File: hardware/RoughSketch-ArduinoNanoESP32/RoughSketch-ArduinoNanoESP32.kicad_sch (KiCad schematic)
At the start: 28 parts, among them J1 Front Panel, K1 Compressor Relay, K2 Auger Relay, M1 Compressor, M2 Auger Motor, M3 Pump, M4 Fan, Q1 Pump Mosfet, Q2 UV LED Mosfet, Q3 Fan Mosfet, Q4 Bin LED Mosfet, Q5 IR LED Mosfet, SW3 Bin Switch, SW4 Float High, SW5 Float Low

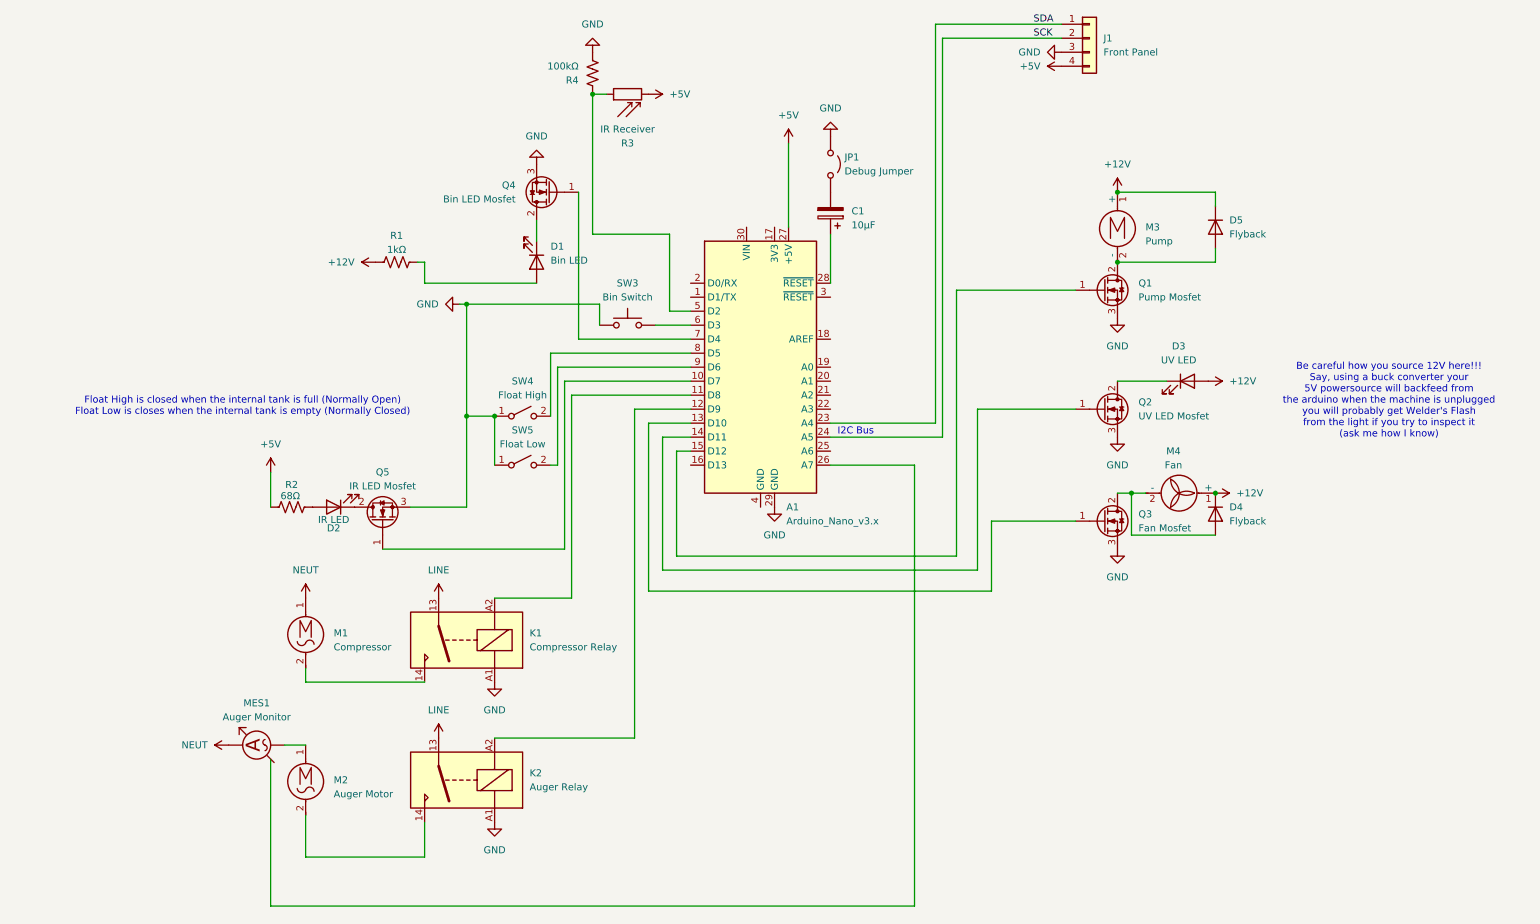
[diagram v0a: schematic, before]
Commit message: Migration from Atmel to ESP32
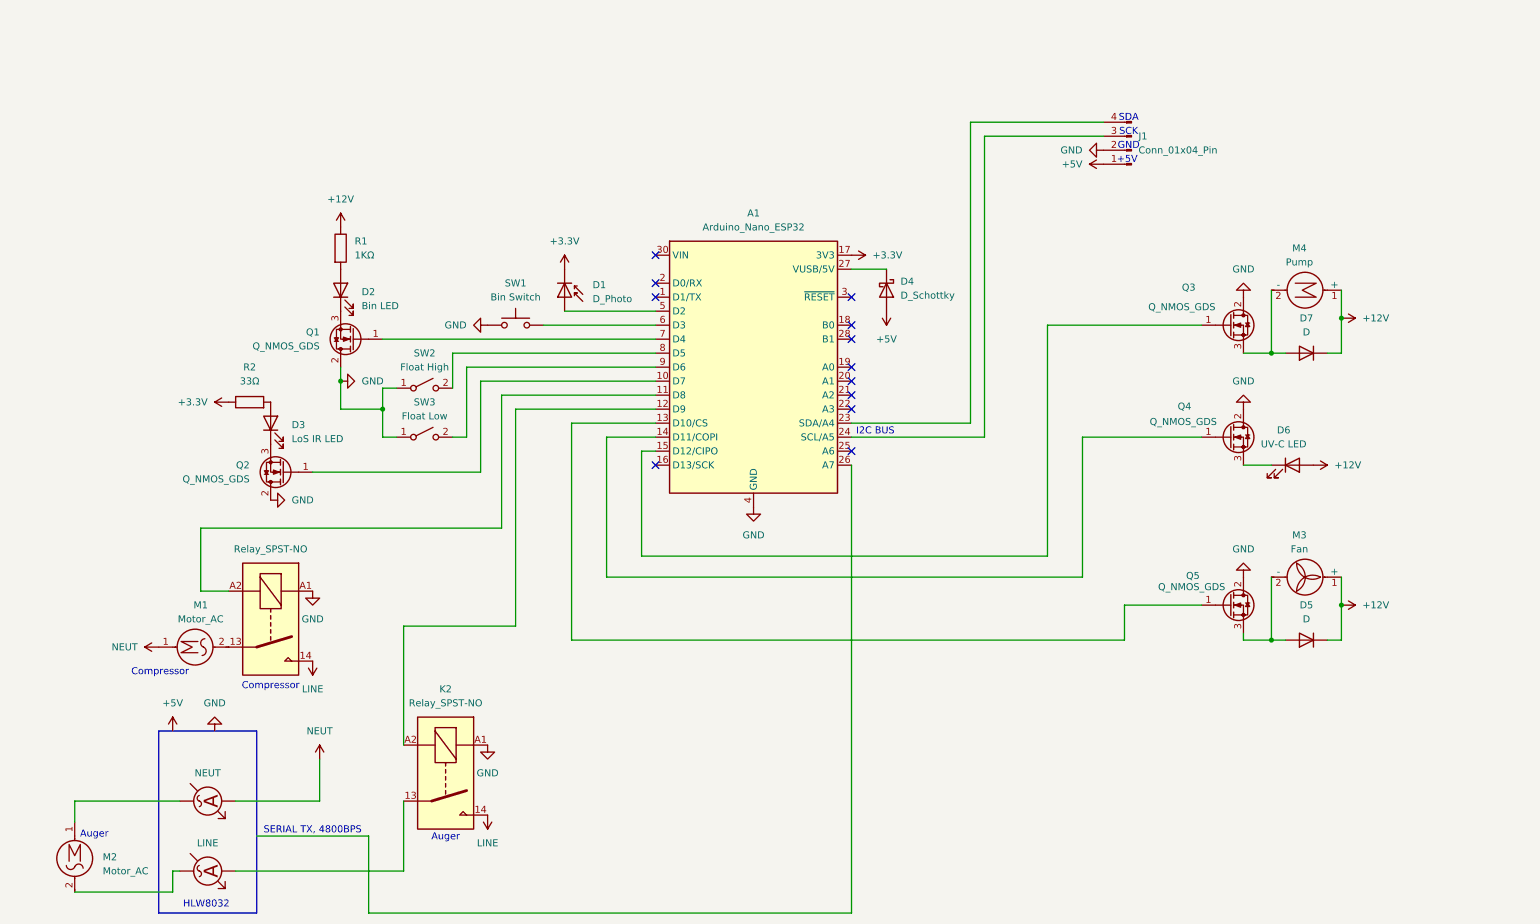
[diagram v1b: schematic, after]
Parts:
- removed A1: Arduino_Nano_v3.x, Module:Arduino_Nano, symbol MCU_Module:Arduino_Nano_v3.x
- removed C1: 10µF, symbol Device:C_Polarized
- removed D1: Bin LED, symbol Device:LED
- removed D4: Flyback, symbol Device:D
- removed J1: Front Panel, symbol Connector_Generic:Conn_01x04
- removed JP1: Debug Jumper, symbol Jumper:Jumper_2_Open
- removed M3: Pump, symbol Motor:Motor_DC
- removed M4: Fan, symbol Motor:Fan
- removed R1: 1kΩ, symbol Device:R_US
- removed R2: 68Ω, symbol Device:R_US
- removed R3: IR Receiver, symbol Device:R_Photo
- removed R4: 100kΩ, symbol Device:R_US
- removed SW3: Bin Switch, symbol Switch:SW_Push
- removed SW4: Float High, symbol Switch:SW_SPST
- removed SW5: Float Low, symbol Switch:SW_SPST
- added A1: Arduino_Nano_ESP32, Module:Arduino_Nano, symbol MCU_Module:Arduino_Nano_ESP32
- added D1: D_Photo, symbol Device:D_Photo
- added D4: D_Schottky, Diode_THT:D_DO-35_SOD27_P7.62mm_Horizontal, symbol Device:D_Schottky
- added D6: UV-C LED, symbol Device:LED
- added D7: D, symbol Device:D
- added J1: Conn_01x04_Pin, Package_DIP:DIP-20_W7.62mm, symbol Connector:Conn_01x04_Pin
- added M3: Fan, symbol Motor:Fan
- added M4: Pump, symbol Motor:Motor_DC
- added MES2: LINE, symbol Device:Ammeter_AC
- added R1: 1KΩ, symbol Device:R
- added R2: 33Ω, symbol Device:R
- added SW1: Bin Switch, Package_DIP:DIP-24_W7.62mm, symbol Switch:SW_Push
- added SW2: Float High, Button_Switch_SMD:SW_SPST_CK_KMS2xxGP, symbol Switch:SW_SPST
- added SW3: Float Low, Button_Switch_SMD:SW_SPST_CK_KMS2xxGP, symbol Switch:SW_SPST
- D2: value IR LED -> Bin LED
- D3: value UV LED -> LoS IR LED
- D5: value Flyback -> D
- K1: value Compressor Relay -> Relay_SPST-NO
- K2: value Auger Relay -> Relay_SPST-NO
- M1: value Compressor -> Motor_AC
- M2: value Auger Motor -> Motor_AC
- MES1: value Auger Monitor -> NEUT
- Q1: value Pump Mosfet -> Q_NMOS_GDS; footprint (none) -> Package_DFN_QFN:NXP_LQFN-48-1EP_7x7mm_P0.5mm_EP3.5x3.5mm_16xMask0.45x0.45_ThermalVias
- Q2: value UV LED Mosfet -> Q_NMOS_GDS; footprint (none) -> Package_DFN_QFN:NXP_LQFN-48-1EP_7x7mm_P0.5mm_EP3.5x3.5mm_16xMask0.45x0.45_ThermalVias
- Q3: value Fan Mosfet -> Q_NMOS_GDS; footprint (none) -> Package_DFN_QFN:NXP_LQFN-48-1EP_7x7mm_P0.5mm_EP3.5x3.5mm_16xMask0.45x0.45_ThermalVias
- Q4: value Bin LED Mosfet -> Q_NMOS_GDS; footprint (none) -> Package_DFN_QFN:NXP_LQFN-48-1EP_7x7mm_P0.5mm_EP3.5x3.5mm_16xMask0.45x0.45_ThermalVias
- Q5: value IR LED Mosfet -> Q_NMOS_GDS; footprint (none) -> Package_DFN_QFN:NXP_LQFN-48-1EP_7x7mm_P0.5mm_EP3.5x3.5mm_16xMask0.45x0.45_ThermalVias
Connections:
- net +12V: now also D6.2 (A), D7.1 (K), M3.1 (+), M4.1 (+), R1.1; no longer D3.2 (A)
- net +5V: now also D4.2 (A), J1.1 (Pin_1)
- net GND: now also Q1.2 (D), Q2.2 (D), Q3.2 (D), Q4.2 (D), Q5.2 (D), A1.29 (GND), A1.4 (GND), J1.2 (Pin_2), SW1.1, SW2.1 (A), SW3.1 (A); no longer Q1.3 (S), Q2.3 (S), Q3.3 (S), Q4.3 (S), Q5.3 (S)
- net LINE: now also K1.14, K2.14; no longer K1.13, K2.13
- net at D5.2 (A): now also Q5.3 (S), M3.2 (-); no longer Q1.2 (D)
- net at Q4.1 (G): now also A1.14 (D11/COPI)
- net at M1.2: now also K1.13; no longer K1.14
- net at K1.A2: now also A1.11 (D8)
- net at Q5.1 (G): now also A1.13 (D10/CS)
- net at D2.1 (K): now also Q1.3 (S); no longer Q5.2 (D)
- net at Q2.1 (G): now also A1.10 (D7)
- net at D3.1 (K): now also Q2.3 (S); no longer Q2.2 (D)
- net at M2.2: now also MES2.1; no longer K2.14
- net at D2.2 (A): now also R1.2
- net at K2.A2: now also A1.12 (D9)
- net at Q3.1 (G): now also A1.15 (D12/CIPO)
- net at Q1.1 (G): now also A1.7 (D4)
- new net: A1.9 (D6), SW3.2 (B)
- new net: D6.1 (K), Q4.3 (S)
- new net: A1.8 (D5), SW2.2 (B)
- new net: A1.6 (D3), SW1.2
- new net: D7.2 (A), M4.2 (-), Q3.3 (S)
- new net: A1.27 (VUSB/5V), D4.1 (K)
- new net: A1.24 (SCL/A5), J1.3 (Pin_3)
- new net: A1.23 (SDA/A4), J1.4 (Pin_4)
- new net: K2.13, MES2.2
- new net: A1.5 (D2), D1.2 (A)
- new net: D3.2 (A), R2.2
- new net +3.3V: A1.17 (3V3), D1.1 (K), R2.1
- no-connect marks 0 -> 12
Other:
- note added: "+5V"
- note added: "Auger"
- note added: "Compressor"
- note added: "GND"
- note added: "HLW8032"
- note added: "I2C BUS"
- note added: "SCK"
- note added: "SDA"
- note added: "SERIAL TX, 4800BPS"
- note removed: "Be careful how you source 12V here!!! Say, using a buck converter your 5V powersource will backfeed from the arduino when the machine is unplugged you will probably get Welder's Flash from the light if you try to inspect it (ask me how I know)"
- note removed: "Float High is closed when the internal tank is full (Normally Open) Float Low is closes when the internal tank is empty (Normally Closed)"
- note removed: "I2C Bus"
- title: GE Opal 2 Board replacement -> GE Opal Ice Machine Replacement Board (ESP32)
